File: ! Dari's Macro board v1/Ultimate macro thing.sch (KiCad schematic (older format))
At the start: 71 parts, among them J1 Conn_02x03_Odd_Even, J2 Conn_01x04, SW1 SW_Push, SW2 SW_Push, SW3 Rotary_Encoder, U1 ATmega328P-PU, Y1 16Mhz

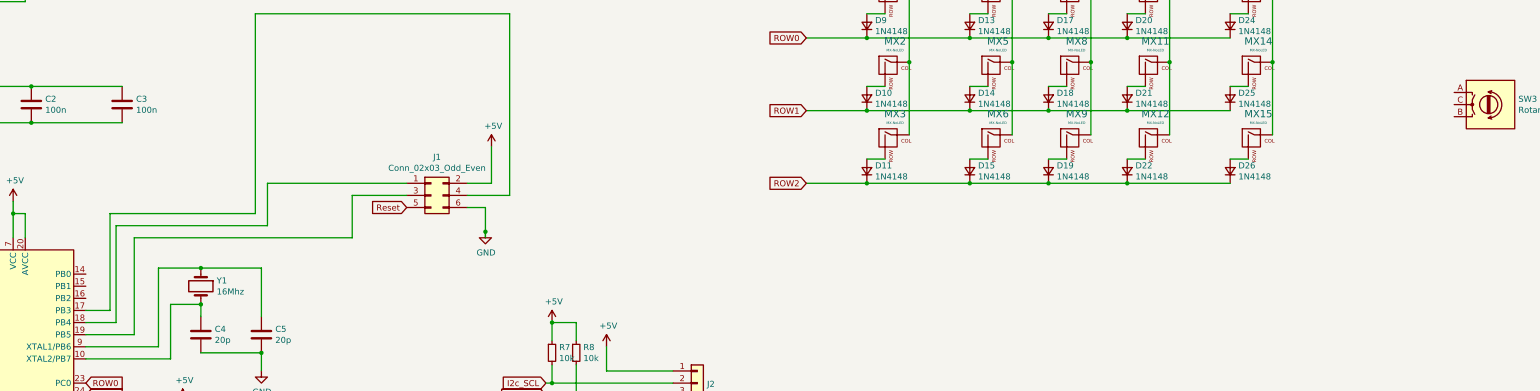
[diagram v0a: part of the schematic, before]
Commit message: Linked encoder
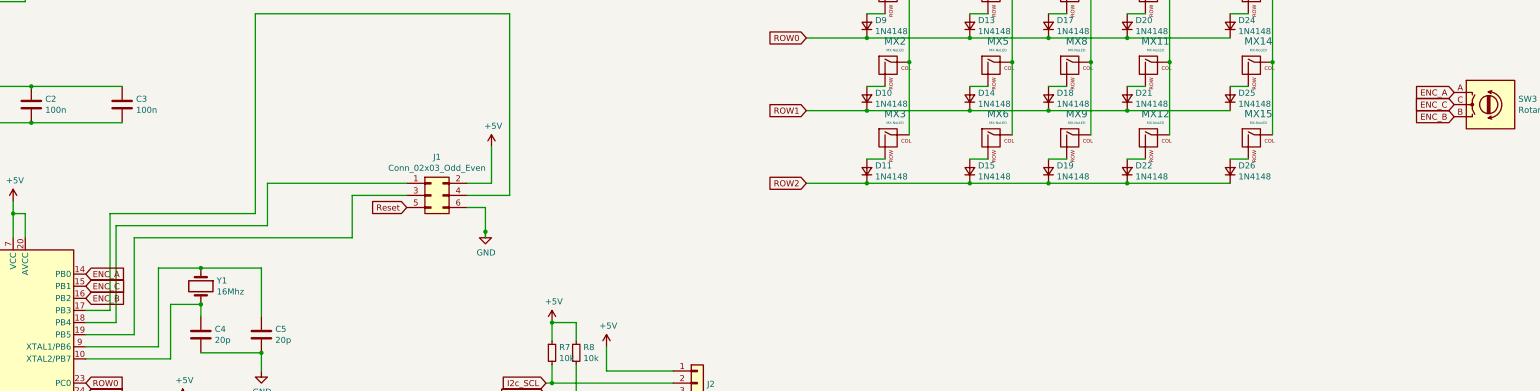
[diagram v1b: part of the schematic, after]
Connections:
- net ENC_A: now reaches U1.14 (PB0)
- net ENC_A: now also SW3.A
- net ENC_C: now reaches U1.15 (PB1)
- net ENC_C: now also SW3.C
- net ENC_B: now reaches U1.16 (PB2)
- net ENC_B: now also SW3.B
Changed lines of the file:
@@
 Wire Wire Line
 	10600 2550 10600 3150
+Text GLabel 14250 3000 0    50   Input ~ 0
+ENC_B
+Text GLabel 2950 4300 2    50   Input ~ 0
+ENC_A
+Text GLabel 14250 2800 0    50   Input ~ 0
+ENC_A
+Text GLabel 14250 2900 0    50   Input ~ 0
+ENC_C
+Text GLabel 2950 4400 2    50   Input ~ 0
+ENC_C
+Text GLabel 2950 4500 2    50   Input ~ 0
+ENC_B
 $EndSCHEMATC

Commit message: Redesign
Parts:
- removed D12, D16, D23, D27, D28, D29, D3, D30, D31, D32, D33, D34, D4, D7, D8: WS2812B, LED_SMD:LED_WS2812B_PLCC4_5.0x5.0mm_P3.2mm, symbol LED:WS2812B
- added R10, R9: 220, Resistor_THT:R_Axial_DIN0204_L3.6mm_D1.6mm_P5.08mm_Horizontal, symbol Device:R_Small
- MX10, MX12, MX14, MX3, MX4, MX8: footprint ! MX bases:MXOnly-1U-NoLED -> ! MX bases:MXOnly-1U; symbol MX_Alps_Hybrid:MX-NoLED -> MX_Alps_Hybrid:MX-LED
- renumbered D24 to D23, D25 to D24, D26 to D25, D5 to D3, D6 to D4, D9 to D5, D10 to D6, D11 to D7
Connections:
- net GND: now also MX10.4 (LEDGND), MX14.4 (LEDGND), MX3.4 (LEDGND), MX4.4 (LEDGND), MX8.4 (LEDGND)
- net RGBINPUT: no longer U1.6 (PD4)
- net ROW0: now also J1.3 (Pin_3), U1.19 (PB5); no longer U1.23 (PC0)
- new net: MX10.3 (LED), MX4.3 (LED), MX8.3 (LED), R9.1
- new net: MX12.3 (LED), MX14.3 (LED), MX3.3 (LED), R10.2
- new net LED1: R9.2, U1.23 (PC0)
- new net LED2: R10.1, U1.6 (PD4)

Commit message: Redesigned pro micro
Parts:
- removed R10: 220, Resistor_THT:R_Axial_DIN0204_L3.6mm_D1.6mm_P5.08mm_Horizontal, symbol Device:R_Small
- added D12, D16, D20, D24, D25, D26, D27, D28, D8: 1N4148, Diode_THT:D_DO-35_SOD27_P7.62mm_Horizontal, symbol Device:D_Small
- added D29, D30, D31, D32, D33, D34, D35, D36, D37, D38, D39, D40, D41, D42, D43, D44, D45, D46, D47, D48, D49, D50, D51, D52: WS2812B, LED_SMD:LED_WS2812B_PLCC4_5.0x5.0mm_P3.2mm, symbol LED:WS2812B
- added MX12, MX16, MX20, MX21, MX22, MX23, MX24, MX4, MX8: MX-NoLED, ! MX bases:MXOnly-1U-NoLED, symbol MX_Alps_Hybrid:MX-NoLED
- MX10: renamed from MX8; footprint ! MX bases:MXOnly-1U -> ! MX bases:MXOnly-1U-NoLED; symbol MX_Alps_Hybrid:MX-LED -> MX_Alps_Hybrid:MX-NoLED
- MX13: renamed from MX10; footprint ! MX bases:MXOnly-1U -> ! MX bases:MXOnly-1U-NoLED; symbol MX_Alps_Hybrid:MX-LED -> MX_Alps_Hybrid:MX-NoLED
- MX15: renamed from MX12; footprint ! MX bases:MXOnly-1U -> ! MX bases:MXOnly-1U-NoLED; symbol MX_Alps_Hybrid:MX-LED -> MX_Alps_Hybrid:MX-NoLED
- MX18: renamed from MX14; footprint ! MX bases:MXOnly-1U -> ! MX bases:MXOnly-1U-NoLED; symbol MX_Alps_Hybrid:MX-LED -> MX_Alps_Hybrid:MX-NoLED
- MX3: footprint ! MX bases:MXOnly-1U -> ! MX bases:MXOnly-1U-NoLED; symbol MX_Alps_Hybrid:MX-LED -> MX_Alps_Hybrid:MX-NoLED
- MX5: renamed from MX4; footprint ! MX bases:MXOnly-1U -> ! MX bases:MXOnly-1U-NoLED; symbol MX_Alps_Hybrid:MX-LED -> MX_Alps_Hybrid:MX-NoLED
- R9: value 220 -> 470
- renumbered D14 to D10, D15 to D11, D17 to D13, D18 to D14, D19 to D15, D20 to D17, D21 to D18, D22 to D19, D23 to D21, D24 to D22, D25 to D23, D13 to D9, MX9 to MX11, MX11 to MX14, MX13 to MX17, MX15 to MX19, MX5 to MX6, MX6 to MX7, MX7 to MX9
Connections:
- net LED1 is gone; now on net RGBINPUT: R9.2, U1.23 (PC0)
- net LED2 is gone; now on net ROW0: U1.6 (PD4)
- net COL0: now also MX4.1 (COL)
- net COL1: now also MX8.1 (COL)
- net COL2: now also MX12.1 (COL)
- net COL3: now also MX16.1 (COL)
- net COL4: now also MX20.1 (COL)
- net GND: now also D29.3 (VSS), D30.3 (VSS), D31.3 (VSS), D32.3 (VSS), D33.3 (VSS), D34.3 (VSS), D35.3 (VSS), D36.3 (VSS), D37.3 (VSS), D38.3 (VSS), D39.3 (VSS), D40.3 (VSS), D41.3 (VSS), D42.3 (VSS), D43.3 (VSS), D44.3 (VSS), D45.3 (VSS), D46.3 (VSS), D47.3 (VSS), D48.3 (VSS), D49.3 (VSS), D50.3 (VSS), D51.3 (VSS), D52.3 (VSS); no longer MX10.4 (LEDGND), MX13.4 (LEDGND), MX18.4 (LEDGND), MX3.4 (LEDGND), MX5.4 (LEDGND)
- net ROW0: now also D25.1 (K); no longer J1.3 (Pin_3), U1.19 (PB5)
- net ROW1: now also D26.1 (K)
- net ROW2: now also D27.1 (K)
- net COL5: now reaches J1.1 (Pin_1), U1.18 (PB4)
- net COL5: now also MX21.1 (COL), MX22.1 (COL), MX23.1 (COL), MX24.1 (COL)
- new net: D30.2 (DOUT), D31.4 (DIN)
- new net: D29.2 (DOUT), D30.4 (DIN)
- new net: D31.2 (DOUT), D32.4 (DIN)
- new net: D29.4 (DIN), R9.1
- new net: D32.2 (DOUT), D33.4 (DIN)
- new net: D33.2 (DOUT), D34.4 (DIN)
- new net: D34.2 (DOUT), D35.4 (DIN)
- new net: D35.2 (DOUT), D36.4 (DIN)
- new net: D36.2 (DOUT), D37.4 (DIN)
- new net: D37.2 (DOUT), D38.4 (DIN)
- new net: D38.2 (DOUT), D39.4 (DIN)
- new net: D39.2 (DOUT), D40.4 (DIN)
- new net: D40.2 (DOUT), D41.4 (DIN)
- new net: D41.2 (DOUT), D42.4 (DIN)
- new net: D42.2 (DOUT), D43.4 (DIN)
- new net: D43.2 (DOUT), D44.4 (DIN)
- new net: D44.2 (DOUT), D45.4 (DIN)
- new net: D45.2 (DOUT), D46.4 (DIN)
- new net: D46.2 (DOUT), D47.4 (DIN)
- new net: D47.2 (DOUT), D48.4 (DIN)
- new net: D48.2 (DOUT), D49.4 (DIN)
- new net: D49.2 (DOUT), D50.4 (DIN)
- new net: D50.2 (DOUT), D51.4 (DIN)
- new net: D51.2 (DOUT), D52.4 (DIN)
- new net: D27.2 (A), MX23.2 (ROW)
- new net: D25.2 (A), MX21.2 (ROW)
- new net: D26.2 (A), MX22.2 (ROW)
- new net: D8.2 (A), MX4.2 (ROW)
- new net: D12.2 (A), MX8.2 (ROW)
- new net: D16.2 (A), MX12.2 (ROW)
- new net: D24.2 (A), MX20.2 (ROW)
- new net: D20.2 (A), MX16.2 (ROW)
- new net: D28.2 (A), MX24.2 (ROW)
- new net -5V: D29.1 (VDD), D30.1 (VDD), D31.1 (VDD), D32.1 (VDD), D33.1 (VDD), D34.1 (VDD), D35.1 (VDD), D36.1 (VDD), D37.1 (VDD), D38.1 (VDD), D39.1 (VDD), D40.1 (VDD), D41.1 (VDD), D42.1 (VDD), D43.1 (VDD), D44.1 (VDD), D45.1 (VDD), D46.1 (VDD), D47.1 (VDD), D48.1 (VDD), D49.1 (VDD), D50.1 (VDD), D51.1 (VDD), D52.1 (VDD)
- new net ROW3: D12.1 (K), D16.1 (K), D20.1 (K), D24.1 (K), D28.1 (K), D8.1 (K), J1.3 (Pin_3), U1.19 (PB5)

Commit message: a
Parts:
- added R? (x2): 470, Resistor_THT:R_Axial_DIN0204_L3.6mm_D1.6mm_P5.08mm_Horizontal, symbol Device:R_Small
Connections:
- net GND: now also SW3.C
- net RGBINPUT2: now reaches J1.4 (Pin_4), U1.17 (PB3)
- net RGBINPUT2: now also R?.2
- net at D35.2 (DOUT): no longer D36.4 (DIN)
- net at D41.2 (DOUT): no longer D42.4 (DIN)
- net ENC_C renamed RGBINPUT1
- net RGBINPUT1: now also R?.2; no longer SW3.C
- new net: D36.4 (DIN), R?.1
- new net: D42.4 (DIN), R?.1
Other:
- moved on the sheet: D36, D37, D38, D39, D40, D41
